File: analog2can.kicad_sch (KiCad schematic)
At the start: 2 parts, among them U1 STM32U535CBTx, U2 TJA1051T-E

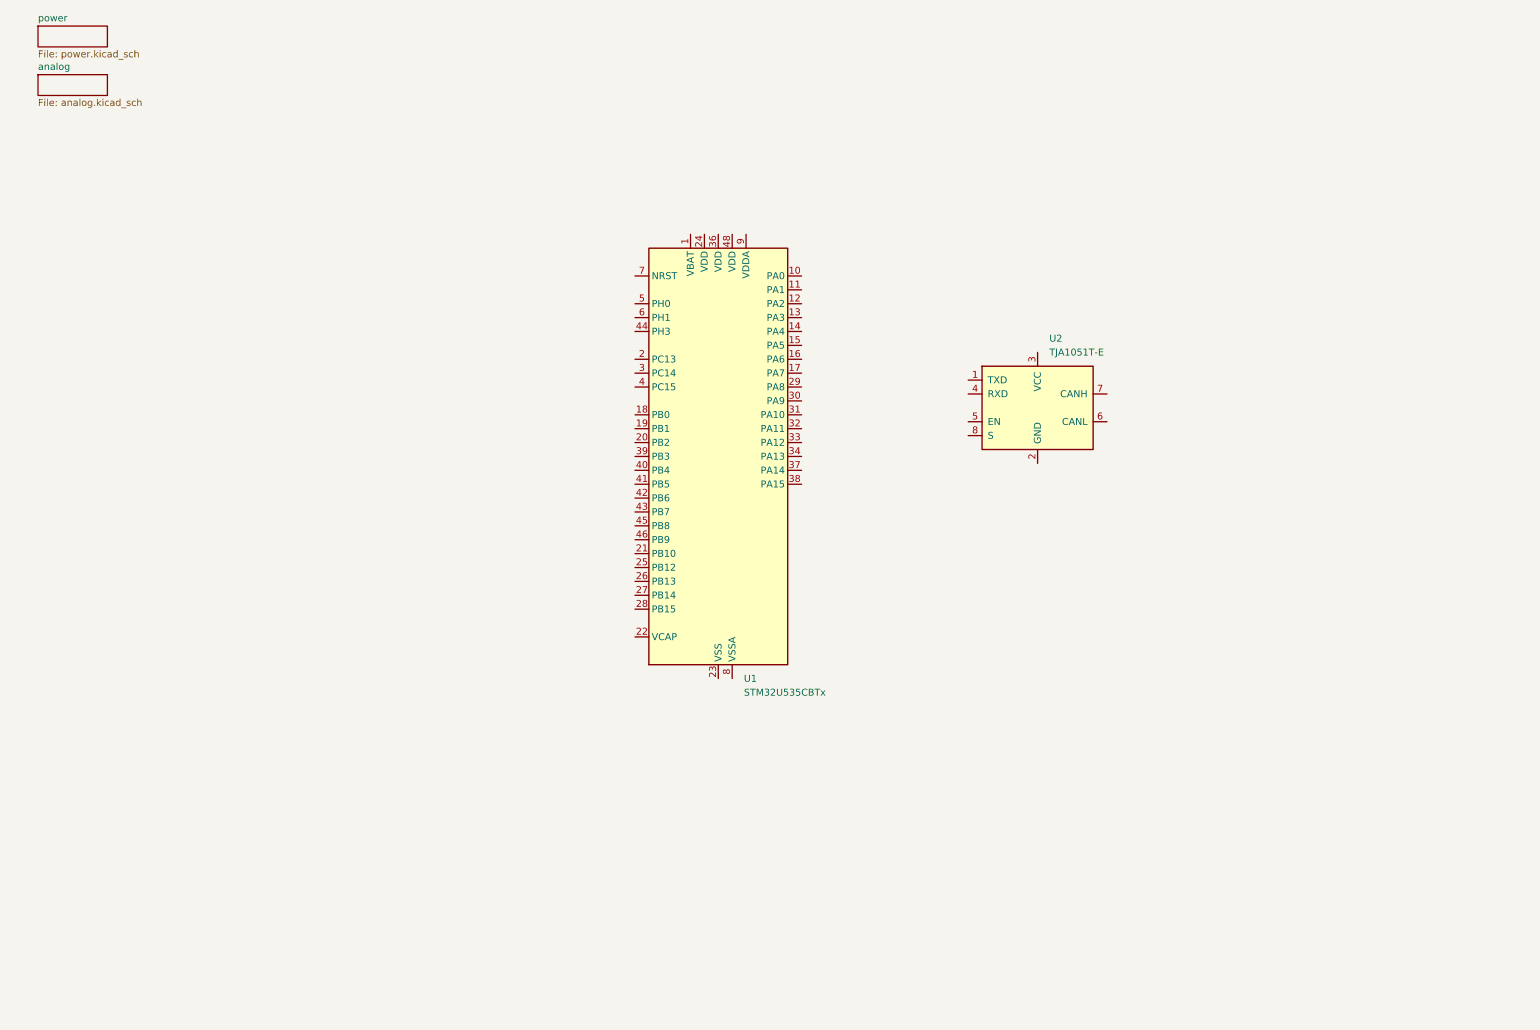
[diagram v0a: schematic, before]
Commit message: Schema devrait etre fini. A revalider avec le layout (Surtout SWO pour debug)
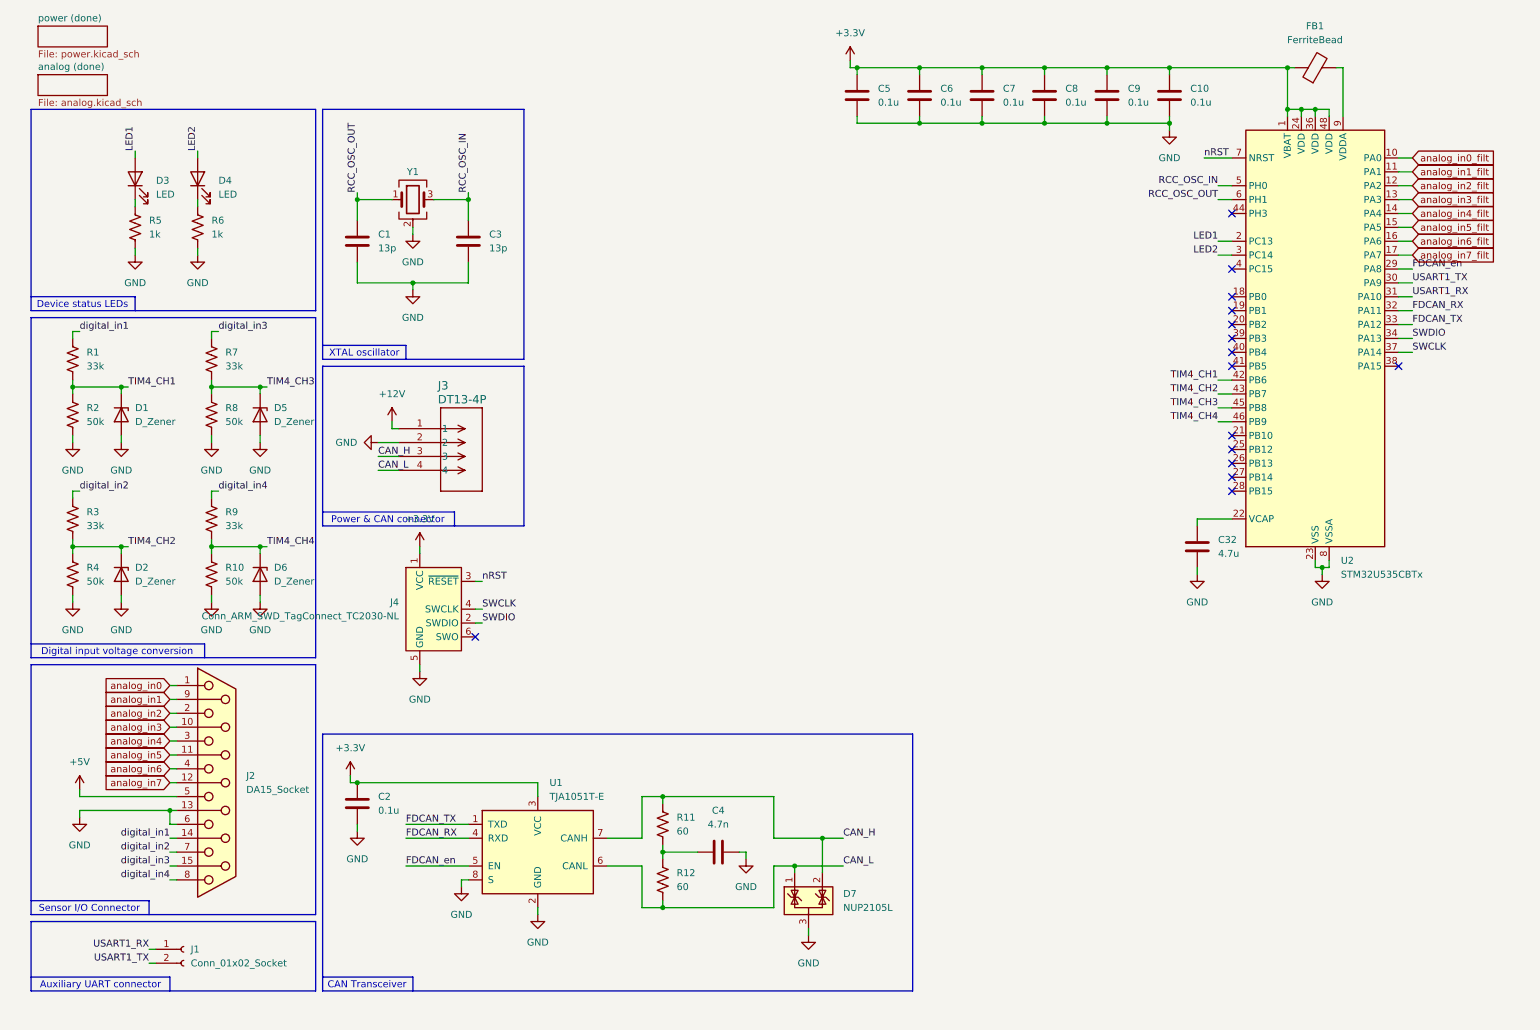
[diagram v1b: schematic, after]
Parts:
- added C1, C3: 13p, Capacitor_SMD:C_0402_1005Metric_Pad0.74x0.62mm_HandSolder, symbol Device:C
- added C10, C2, C5, C6, C7, C8, C9: 0.1u, Capacitor_SMD:C_0402_1005Metric_Pad0.74x0.62mm_HandSolder, symbol Device:C
- added C32: 4.7u, Capacitor_SMD:C_0603_1608Metric_Pad1.08x0.95mm_HandSolder, symbol Device:C
- added C4: 4.7n, Capacitor_SMD:C_0402_1005Metric_Pad0.74x0.62mm_HandSolder, symbol Device:C
- added D1, D2, D5, D6: D_Zener, Diode_SMD:D_SOD-323, symbol Device:D_Zener
- added D3, D4: LED, LED_SMD:LED_0603_1608Metric_Pad1.05x0.95mm_HandSolder, symbol Device:LED
- added D7: NUP2105L, Package_TO_SOT_SMD:SOT-23, symbol Power_Protection:NUP2105L
- added FB1: FerriteBead, Inductor_SMD:L_0402_1005Metric_Pad0.77x0.64mm_HandSolder, symbol Device:FerriteBead
- added J1: Conn_01x02_Socket, Connector_PinHeader_1.00mm:PinHeader_2x31_P1.00mm_Horizontal, symbol Connector:Conn_01x02_Socket
- added J2: DA15_Socket, Connector_Dsub:DSUB-15_Socket_Horizontal_P2.77x2.84mm_EdgePinOffset4.94mm_Housed_MountingHolesOffset4.94mm, symbol Connector:DA15_Socket
- added J3: DT13-4P, DT13-4P:CONN4_DT13-4P_TEC, symbol DT13-4P:DT13-4P
- added J4: Conn_ARM_SWD_TagConnect_TC2030-NL, Connector:Tag-Connect_TC2030-IDC-NL_2x03_P1.27mm_Vertical, symbol Connector:Conn_ARM_SWD_TagConnect_TC2030-NL
- added R1, R3, R7, R9: 33k, Resistor_SMD:R_0603_1608Metric_Pad0.98x0.95mm_HandSolder, symbol Device:R_US
- added R10, R2, R4, R8: 50k, Resistor_SMD:R_0603_1608Metric_Pad0.98x0.95mm_HandSolder, symbol Device:R_US
- added R11, R12: 60, Resistor_SMD:R_0603_1608Metric_Pad0.98x0.95mm_HandSolder, symbol Device:R_US
- added R5, R6: 1k, Resistor_SMD:R_0603_1608Metric_Pad0.98x0.95mm_HandSolder, symbol Device:R_US
- added Y1: ABM8-16.000MHZ-D1X-T, Crystal:Crystal_SMD_Abracon_ABM8G-4Pin_3.2x2.5mm, symbol Device:Crystal_GND24
- renumbered U2 to U1, U1 to U2
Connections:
- net +3.3V: now reaches U2.1 (VBAT)
- net +3.3V: now also U1.3 (VCC), U2.24 (VDD), U2.36 (VDD), U2.48 (VDD), C10.1, C2.1, C5.1, C6.1, C7.1, C8.1, C9.1, FB1.1, J4.1 (VCC)
- net analog_in0_filt: now reaches U2.10 (PA0)
- net analog_in1_filt: now reaches U2.11 (PA1)
- net analog_in2_filt: now reaches U2.12 (PA2)
- net analog_in3_filt: now reaches U2.13 (PA3)
- net analog_in4_filt: now reaches U2.14 (PA4)
- net analog_in5_filt: now reaches U2.15 (PA5)
- net analog_in6_filt: now reaches U2.16 (PA6)
- net analog_in7_filt: now reaches U2.17 (PA7)
- net LED1: now reaches U2.2 (PC13)
- net LED1: now also D3.2 (A)
- net at U2.22 (VCAP): now also C32.1
- net GND: now reaches U2.23 (VSS), U2.35 (VSS), U2.47 (VSS)
- net GND: now also U1.2 (GND), U1.8 (S), U2.8 (VSSA), C1.2, C10.2, C2.2, C3.2, C32.2, C4.2, C5.2, C6.2, C7.2, C8.2, C9.2, D1.2 (A), D2.2 (A), D5.2 (A), D6.2 (A), D7.3 (A), J2.13 (P13), J2.6, J3.2, J4.5 (GND), R10.2, R2.2, R4.2, R5.2, R6.2, R8.2, Y1.2 (G), Y1.4 (G)
- net FDCAN_en: now reaches U2.29 (PA8)
- net FDCAN_en: now also U1.5 (EN)
- net LED2: now reaches U2.3 (PC14)
- net LED2: now also D4.2 (A)
- net USART1_TX: now reaches U2.30 (PA9)
- net USART1_TX: now also J1.2 (Pin_2)
- net USART1_RX: now reaches U2.31 (PA10)
- net USART1_RX: now also J1.1 (Pin_1)
- net FDCAN_RX: now reaches U2.32 (PA11)
- net FDCAN_RX: now also U1.4 (RXD)
- net FDCAN_TX: now reaches U2.33 (PA12)
- net FDCAN_TX: now also U1.1 (TXD)
- net SWDIO: now reaches U2.34 (PA13)
- net SWDIO: now also J4.2 (SWDIO)
- net SWCLK: now reaches U2.37 (PA14)
- net SWCLK: now also J4.4 (SWCLK)
- net TIM4_CH1: now reaches U2.42 (PB6)
- net TIM4_CH1: now also D1.1 (K), R1.2, R2.1
- net TIM4_CH2: now reaches U2.43 (PB7)
- net TIM4_CH2: now also D2.1 (K), R3.2, R4.1
- net TIM4_CH3: now reaches U2.45 (PB8)
- net TIM4_CH3: now also D5.1 (K), R7.2, R8.1
- net TIM4_CH4: now reaches U2.46 (PB9)
- net TIM4_CH4: now also D6.1 (K), R10.1, R9.2
- net RCC_OSC_IN: now reaches U2.5 (PH0)
- net RCC_OSC_IN: now also C3.1, Y1.3
- net RCC_OSC_OUT: now reaches U2.6 (PH1)
- net RCC_OSC_OUT: now also C1.1, Y1.1
- net nRST: now reaches U2.7 (NRST)
- net nRST: now also J4.3 (~{RESET})
- net at U2.9 (VDDA): now also FB1.2
- net CAN_L: now reaches U1.6 (CANL)
- net CAN_L: now also D7.1 (K), J3.4, R12.2
- net CAN_H: now reaches U1.7 (CANH)
- net CAN_H: now also D7.2 (K), J3.3, R11.1
- new net: C4.1, R11.2, R12.1
- new net: D4.1 (K), R6.1
- new net: D3.1 (K), R5.1
- new net +12V: J3.1
- new net +5V: J2.5
- new net analog_in0: J2.1
- new net analog_in1: J2.9 (P9)
- new net analog_in2: J2.2
- new net analog_in3: J2.10 (P10)
- new net analog_in4: J2.3
- new net analog_in5: J2.11 (P111)
- new net analog_in6: J2.4
- new net analog_in7: J2.12 (P12)
- new net digital_in1: J2.14 (P14), R1.1
- new net digital_in2: J2.7, R3.1
- new net digital_in3: J2.15 (P15), R7.1
- new net digital_in4: J2.8, R9.1
- no-connect marks 0 -> 15
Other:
- sheet analog renamed analog (done)
- sheet power renamed power (done)
- note added: "Auxiliary UART connector"
- note added: "CAN Transceiver"
- note added: "Device status LEDs"
- note added: "Digital input voltage conversion"
- note added: "Power & CAN connector"
- note added: "Sensor I/O Connector"
- note added: "XTAL oscillator"
- moved on the sheet: U1, U2

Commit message: Debut layout PCB et review Schema done
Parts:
- removed J1: Conn_01x02_Socket, Connector_PinHeader_1.00mm:PinHeader_2x31_P1.00mm_Horizontal, symbol Connector:Conn_01x02_Socket
- added J1: Conn_01x04, Connector_Molex:Molex_KK-254_AE-6410-04A_1x04_P2.54mm_Vertical, symbol Connector_Generic:Conn_01x04
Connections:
- net +3.3V: now also J1.3 (Pin_3)
- net GND: now also J1.4 (Pin_4)
- net USART1_RX: now also J1.1 (Pin_1)
- net USART1_TX: now also J1.2 (Pin_2)
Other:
- moved on the sheet: C2, C4, D7, J4, R11, R12, U1

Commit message: fin layout power supply (sauf LDO), debut layout MCU
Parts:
- removed C10: 0.1u, Capacitor_SMD:C_0402_1005Metric_Pad0.74x0.62mm_HandSolder, symbol Device:C
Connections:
- net +3.3V: no longer C2.1, U1.3 (VCC)
- net +5V: now also C2.1, U1.3 (VCC)
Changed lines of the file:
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@@
 	)
 	(junction
-		(at 220.98 33.02)
+		(at 128.27 181.61)
 		(diameter 0)
 		(color 0 0 0 0)
@@
 	)
 	(junction
-		(at 128.27 181.61)
-		(diameter 0)
-		(color 0 0 0 0)
-	)
-	(junction
 		(at 175.26 33.02)
 		(diameter 0)
@@
 	)
 	(junction
-		(at 209.55 22.86)
-		(diameter 0)
-		(color 0 0 0 0)
-	)
-	(junction
 		(at 209.55 33.02)
 		(diameter 0)
@@
 	)
 	(junction
-		(at 220.98 22.86)
+		(at 72.39 158.75)
 		(diameter 0)
 		(color 0 0 0 0)
 	)
 	(junction
-		(at 72.39 158.75)
+		(at 209.55 22.86)
 		(diameter 0)
 		(color 0 0 0 0)
@@
 	(wire
 		(pts
-			(xy 242.57 22.86) (xy 242.57 30.48)
-		)
-		(stroke
-			(width 0)
-			(type default)
-		)
-	)
-	(wire
-		(pts
 			(xy 175.26 33.02) (xy 186.69 33.02)
 		)
@@
 	(wire
 		(pts
-			(xy 209.55 33.02) (xy 220.98 33.02)
-		)
-		(stroke
-			(width 0)
-			(type default)
-		)
-	)
-	(wire
-		(pts
 			(xy 198.12 33.02) (xy 209.55 33.02)
 		)
@@
 	(wire
 		(pts
-			(xy 220.98 24.13) (xy 220.98 22.86)
-		)
-		(stroke
-			(width 0)
-			(type default)
-		)
-	)
-	(wire
-		(pts
 			(xy 20.32 81.28) (xy 20.32 82.55)
 		)
@@
 	(wire
 		(pts
-			(xy 220.98 22.86) (xy 242.57 22.86)
-		)
-		(stroke
-			(width 0)
-			(type default)
-		)
-	)
-	(wire
-		(pts
 			(xy 128.27 171.45) (xy 128.27 172.72)
 		)
@@
 	(wire
 		(pts
-			(xy 209.55 22.86) (xy 220.98 22.86)
-		)
-		(stroke
-			(width 0)
-			(type default)
-		)
-	)
-	(wire
-		(pts
 			(xy 81.28 168.91) (xy 92.71 168.91)
 		)
@@
 	(wire
 		(pts
-			(xy 220.98 33.02) (xy 220.98 31.75)
+			(xy 209.55 22.86) (xy 242.57 22.86)
 		)
 		(stroke
@@
 	(wire
 		(pts
+			(xy 242.57 22.86) (xy 242.57 30.48)
+		)
+		(stroke
+			(width 0)
+			(type default)
+		)
+	)
+	(wire
+		(pts
 			(xy 43.18 46.99) (xy 43.18 48.26)
 		)
@@
 	(wire
 		(pts
-			(xy 220.98 33.02) (xy 220.98 34.29)
+			(xy 209.55 33.02) (xy 209.55 34.29)
 		)
 		(stroke
@@
 	)
 	(symbol
-		(lib_id "Device:C")
-		(at 220.98 27.94 0)
-		(unit 1)
-		(body_style 1)
-		(exclude_from_sim no)
-		(in_bom yes)
-		(on_board yes)
-		(in_pos_files yes)
-		(dnp no)
-		(fields_autoplaced yes)
-		(property "Reference" "C10"
-			(at 224.79 26.6699 0)
-			(show_name no)
-			(do_not_autoplace no)
-			(effects
-				(font
-					(size 1.27 1.27)
-				)
-				(justify left)
-			)
-		)
-		(property "Value" "0.1u"
-			(at 224.79 29.2099 0)
-			(show_name no)
-			(do_not_autoplace no)
-			(effects
-				(font
-					(size 1.27 1.27)
-				)
-				(justify left)
-			)
-		)
-		(property "Footprint" "Capacitor_SMD:C_0402_1005Metric_Pad0.74x0.62mm_HandSolder"
-			(at 221.9452 31.75 0)
-			(hide yes)
-			(show_name no)
-			(do_not_autoplace no)
-			(effects
-				(font
-					(size 1.27 1.27)
-				)
-			)
-		)
-		(property "Datasheet" ""
-			(at 220.98 27.94 0)
-			(hide yes)
-			(show_name no)
-			(do_not_autoplace no)
-			(effects
-				(font
-					(size 1.27 1.27)
-				)
-			)
-		)
-		(property "Description" "Unpolarized capacitor"
-			(at 220.98 27.94 0)
-			(hide yes)
-			(show_name no)
-			(do_not_autoplace no)
-			(effects
-				(font
-					(size 1.27 1.27)
-				)
-			)
-		)
-		(pin "2"
-		)
-		(pin "1"
-		)
-		(instances
-			(project "analog2can"
-				(path "/83888944-f662-44d6-9bff-94055f87dd66"
-					(reference "C10")
-					(unit 1)
-				)
-			)
-		)
-	)
-	(symbol
 		(lib_id "power:GND")
 		(at 29.21 120.65 0)
@@
 	(symbol
 		(lib_id "power:GND")
-		(at 220.98 34.29 0)
+		(at 209.55 34.29 0)
 		(unit 1)
 		(body_style 1)
@@
 		(fields_autoplaced yes)
 		(property "Reference" "#PWR024"
-			(at 220.98 40.64 0)
+			(at 209.55 40.64 0)
 			(hide yes)
 			(show_name no)
@@
 		)
 		(property "Value" "GND"
-			(at 220.98 39.37 0)
+			(at 209.55 39.37 0)
 			(show_name no)
 			(do_not_autoplace no)
@@
 		)
 		(property "Footprint" ""
-			(at 220.98 34.29 0)
+			(at 209.55 34.29 0)
 			(hide yes)
 			(show_name no)
@@
 		)
 		(property "Datasheet" ""
-			(at 220.98 34.29 0)
+			(at 209.55 34.29 0)
 			(hide yes)
 			(show_name no)
@@
 		)
 		(property "Description" "Power symbol creates a global label with name \"GND\" , ground"
-			(at 220.98 34.29 0)
+			(at 209.55 34.29 0)
 			(hide yes)
 			(show_name no)
@@
 	)
 	(symbol
-		(lib_id "power:+3.3V")
-		(at 71.12 157.48 0)
+		(lib_id "power:GND")
+		(at 91.44 177.8 0)
 		(unit 1)
 		(body_style 1)
@@
 		(dnp no)
 		(fields_autoplaced yes)
-		(property "Reference" "#PWR013"
-			(at 71.12 161.29 0)
+		(property "Reference" "#PWR019"
+			(at 91.44 184.15 0)
 			(hide yes)
 			(show_name no)
@@
 			)
 		)
-		(property "Value" "+3.3V"
-			(at 71.12 152.4 0)
+		(property "Value" "GND"
+			(at 91.44 182.88 0)
 			(show_name no)
 			(do_not_autoplace no)
@@
 		)
 		(property "Footprint" ""
-			(at 71.12 157.48 0)
+			(at 91.44 177.8 0)
 			(hide yes)
 			(show_name no)
@@
 		)
 		(property "Datasheet" ""
-			(at 71.12 157.48 0)
+			(at 91.44 177.8 0)
 			(hide yes)
 			(show_name no)
@@
 			)
 		)
-		(property "Description" "Power symbol creates a global label with name \"+3.3V\""
-			(at 71.12 157.48 0)
+		(property "Description" "Power symbol creates a global label with name \"GND\" , ground"
+			(at 91.44 177.8 0)
 			(hide yes)
 			(show_name no)
@@
 			(project "analog2can"
 				(path "/83888944-f662-44d6-9bff-94055f87dd66"
-					(reference "#PWR013")
+					(reference "#PWR019")
 					(unit 1)
 				)
@@
 	)
 	(symbol
-		(lib_id "power:GND")
-		(at 91.44 177.8 0)
+		(lib_id "Device:R_US")
+		(at 45.72 86.36 0)
 		(unit 1)
 		(body_style 1)
@@
 		(dnp no)
 		(fields_autoplaced yes)
-		(property "Reference" "#PWR019"
-			(at 91.44 184.15 0)
-			(hide yes)
+		(property "Reference" "R8"
+			(at 48.26 85.0899 0)
 			(show_name no)
 			(do_not_autoplace no)
@@
 					(size 1.27 1.27)
 				)
+				(justify left)
 			)
 		)
-		(property "Value" "GND"
-			(at 91.44 182.88 0)
+		(property "Value" "50k"
+			(at 48.26 87.6299 0)
 			(show_name no)
 			(do_not_autoplace no)
@@
 					(size 1.27 1.27)
 				)
+				(justify left)
 			)
 		)
-		(property "Footprint" ""
-			(at 91.44 177.8 0)
+		(property "Footprint" "Resistor_SMD:R_0603_1608Metric_Pad0.98x0.95mm_HandSolder"
+			(at 46.736 86.614 90)
 			(hide yes)
 			(show_name no)
@@
 		)
 		(property "Datasheet" ""
-			(at 91.44 177.8 0)
+			(at 45.72 86.36 0)
 			(hide yes)
 			(show_name no)
@@
 			)
 		)
-		(property "Description" "Power symbol creates a global label with name \"GND\" , ground"
-			(at 91.44 177.8 0)
+		(property "Description" "Resistor, US symbol"
+			(at 45.72 86.36 0)
 			(hide yes)
 			(show_name no)
@@
 		(pin "1"
 		)
+		(pin "2"
+		)
 		(instances
 			(project "analog2can"
 				(path "/83888944-f662-44d6-9bff-94055f87dd66"
-					(reference "#PWR019")
+					(reference "R8")
 					(unit 1)
 				)
@@
 	)
 	(symbol
-		(lib_id "Device:R_US")
-		(at 45.72 86.36 0)
+		(lib_id "power:+5V")
+		(at 71.12 157.48 0)
 		(unit 1)
 		(body_style 1)
@@
 		(dnp no)
 		(fields_autoplaced yes)
-		(property "Reference" "R8"
-			(at 48.26 85.0899 0)
+		(property "Reference" "#PWR013"
+			(at 71.12 161.29 0)
+			(hide yes)
 			(show_name no)
 			(do_not_autoplace no)
@@
 					(size 1.27 1.27)
 				)
-				(justify left)
 			)
 		)
-		(property "Value" "50k"
-			(at 48.26 87.6299 0)
+		(property "Value" "+5V"
+			(at 71.12 152.4 0)
 			(show_name no)
 			(do_not_autoplace no)
@@
 					(size 1.27 1.27)
 				)
-				(justify left)
 			)
 		)
-		(property "Footprint" "Resistor_SMD:R_0603_1608Metric_Pad0.98x0.95mm_HandSolder"
-			(at 46.736 86.614 90)
+		(property "Footprint" ""
+			(at 71.12 157.48 0)
 			(hide yes)
 			(show_name no)
@@
 		)
 		(property "Datasheet" ""
-			(at 45.72 86.36 0)
+			(at 71.12 157.48 0)
 			(hide yes)
 			(show_name no)
@@
 			)
 		)
-		(property "Description" "Resistor, US symbol"
-			(at 45.72 86.36 0)
+		(property "Description" "Power symbol creates a global label with name \"+5V\""
+			(at 71.12 157.48 0)
 			(hide yes)
 			(show_name no)
@@
 		(pin "1"
 		)
-		(pin "2"
-		)
 		(instances
 			(project "analog2can"
 				(path "/83888944-f662-44d6-9bff-94055f87dd66"
-					(reference "R8")
+					(reference "#PWR013")
 					(unit 1)
 				)
